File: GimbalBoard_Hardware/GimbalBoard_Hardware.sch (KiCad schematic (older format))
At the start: 5 parts

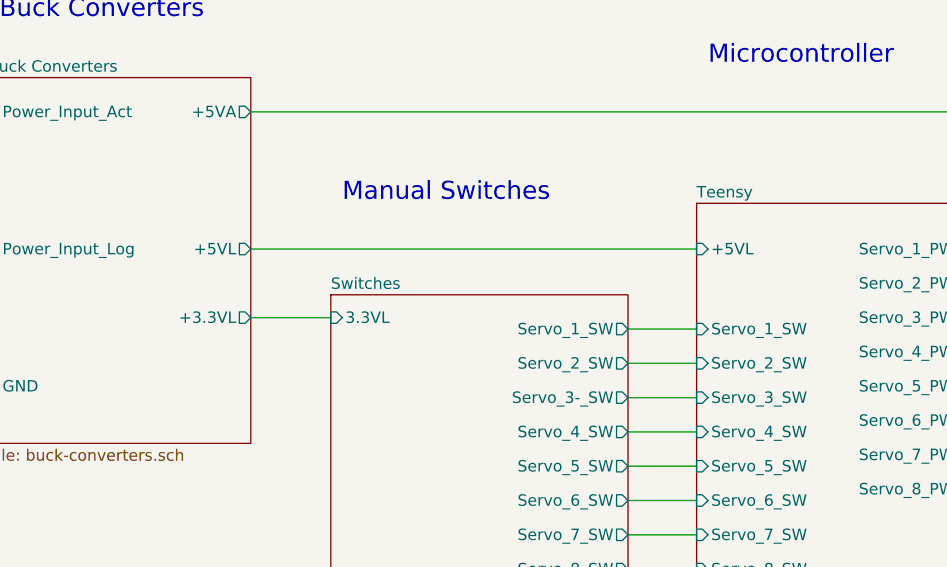
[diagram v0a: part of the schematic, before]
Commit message: now powering the teensy w 3.3VL instead of 5VL
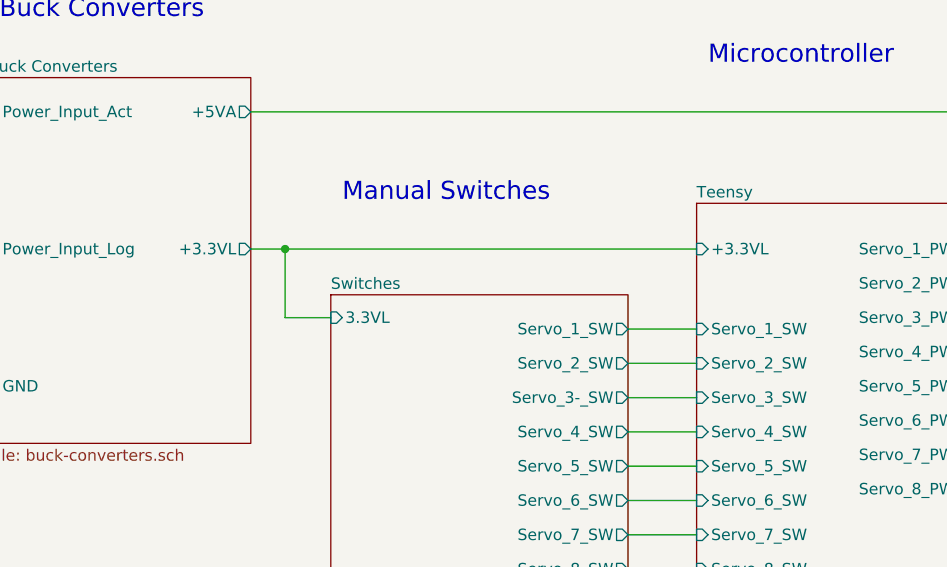
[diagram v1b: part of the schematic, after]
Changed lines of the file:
@@
 F16 "Servo_7_SW" I L 6800 3650 50
 F17 "Servo_8_SW" I L 6800 3800 50
-F18 "+5VL" I L 6800 2400 50
-F19 "Servo_Manual_Control_Right" I L 6800 4300 50
-F20 "Servo_Manual_Control_Left" I L 6800 4150 50
-F21 "GND" I L 6800 4900 50
+F18 "Servo_Manual_Control_Right" I L 6800 4300 50
+F19 "Servo_Manual_Control_Left" I L 6800 4150 50
+F20 "GND" I L 6800 4900 50
+F21 "+3.3VL" I L 6800 2400 50
 $EndSheet
 Wire Wire Line
@@
 	8400 5400 6550 5400
 Wire Wire Line
-	4850 2700 5200 2700
-Wire Wire Line
-	4850 2400 6800 2400
-Wire Wire Line
 	4850 1800 8400 1800
 Wire Wire Line
@@
 Text Notes 8700 1800 0    79   ~ 0
 Servo Connectors
-$Sheet
-S 3700 1650 1150 1600
-U 616B938E
-F0 "Buck Converters" 50
-F1 "buck-converters.sch" 50
-F2 "Power_Input_Act" I L 3700 1800 50
-F3 "+5VL" O R 4850 2400 50
-F4 "+3.3VL" O R 4850 2700 50
-F5 "Power_Input_Log" I L 3700 2400 50
-F6 "GND" I L 3700 3000 50
-F7 "+5VA" O R 4850 1800 50
-$EndSheet
 $Sheet
 S 8700 2100 950  1900
@@
 F11 "GND" I L 8700 3650 50
 $EndSheet
+$Sheet
+S 3700 1650 1150 1600
+U 616B938E
+F0 "Buck Converters" 50
+F1 "buck-converters.sch" 50
+F2 "Power_Input_Act" I L 3700 1800 50
+F3 "+3.3VL" O R 4850 2400 50
+F4 "Power_Input_Log" I L 3700 2400 50
+F5 "GND" I L 3700 3000 50
+F6 "+5VA" O R 4850 1800 50
+$EndSheet
+Wire Wire Line
+	4850 2400 5000 2400
+Wire Wire Line
+	5000 2400 5000 2700
+Wire Wire Line
+	5000 2700 5200 2700
+Connection ~ 5000 2400
+Wire Wire Line
+	5000 2400 6800 2400
 $EndSCHEMATC

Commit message: Added more footprints
I added more footprints. Not done yet. I'd like to come back when when I can verify with max about some of the other components.
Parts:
- D25, D26: footprint (none) -> Diode_SMD:D_0201_0603Metric_Pad0.64x0.40mm_HandSolder
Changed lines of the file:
@@
 F 0 "D25" V 2804 2130 50  0000 L CNN
 F 1 "D_Zener" V 2895 2130 50  0000 L CNN
-F 2 "" H 2850 2050 50  0001 C CNN
+F 2 "Diode_SMD:D_0201_0603Metric_Pad0.64x0.40mm_HandSolder" H 2850 2050 50  0001 C CNN
 F 3 "~" H 2850 2050 50  0001 C CNN
 	1    2850 2050
@@
 F 0 "D26" V 2954 2730 50  0000 L CNN
 F 1 "D_Zener" V 3045 2730 50  0000 L CNN
-F 2 "" H 3000 2650 50  0001 C CNN
+F 2 "Diode_SMD:D_0201_0603Metric_Pad0.64x0.40mm_HandSolder" H 3000 2650 50  0001 C CNN
 F 3 "~" H 3000 2650 50  0001 C CNN
 	1    3000 2650

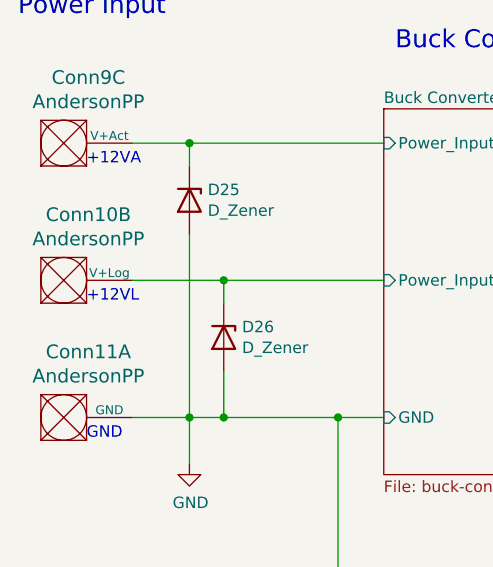
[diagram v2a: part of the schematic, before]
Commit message: Footprints finished
the footprints are finished. the RJ45 connector has been added for eithernet.
the net is in the layout thing but I haven't moved anything yet
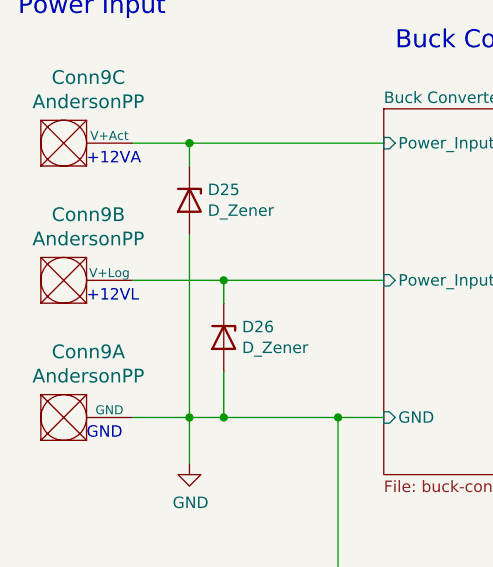
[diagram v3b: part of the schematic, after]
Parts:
- Conn9: footprint (none) -> MRDT_Connectors:Anderson_3_Horizontal_Side_by_Side
- Conn9: renamed from Conn10; footprint (none) -> MRDT_Connectors:Anderson_3_Horizontal_Side_by_Side
- Conn9: renamed from Conn11; footprint (none) -> MRDT_Connectors:Anderson_3_Horizontal_Side_by_Side
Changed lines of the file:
@@
 F 0 "Conn9" H 2408 2287 60  0000 C CNN
 F 1 "AndersonPP" H 2408 2181 60  0000 C CNN
-F 2 "" H 2050 1350 60  0001 C CNN
+F 2 "MRDT_Connectors:Anderson_3_Horizontal_Side_by_Side" H 2050 1350 60  0001 C CNN
 F 3 "" H 2050 1350 60  0001 C CNN
 	3    2200 1900
@@
 $EndComp
 $Comp
-L MRDT_Connectors:AndersonPP Conn10
+L MRDT_Connectors:AndersonPP Conn9
 U 2 1 6159E8BE
 P 2200 2500
-F 0 "Conn10" H 2408 2887 60  0000 C CNN
+F 0 "Conn9" H 2408 2887 60  0000 C CNN
 F 1 "AndersonPP" H 2408 2781 60  0000 C CNN
-F 2 "" H 2050 1950 60  0001 C CNN
+F 2 "MRDT_Connectors:Anderson_3_Horizontal_Side_by_Side" H 2050 1950 60  0001 C CNN
 F 3 "" H 2050 1950 60  0001 C CNN
 	2    2200 2500
@@
 $EndComp
 $Comp
-L MRDT_Connectors:AndersonPP Conn11
+L MRDT_Connectors:AndersonPP Conn9
 U 1 1 6159ED2C
 P 2200 3100
-F 0 "Conn11" H 2408 3487 60  0000 C CNN
+F 0 "Conn9" H 2408 3487 60  0000 C CNN
 F 1 "AndersonPP" H 2408 3381 60  0000 C CNN
-F 2 "" H 2050 2550 60  0001 C CNN
+F 2 "MRDT_Connectors:Anderson_3_Horizontal_Side_by_Side" H 2050 2550 60  0001 C CNN
 F 3 "" H 2050 2550 60  0001 C CNN
 	1    2200 3100

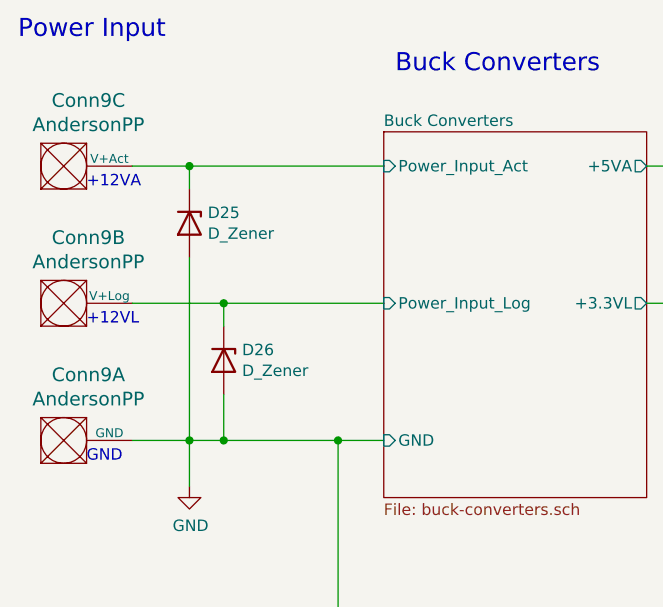
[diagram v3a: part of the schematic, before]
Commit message: ethernet fixed.
the ethernet is fixed. as well as the switch footprint association issue.
I'm not certain that the current footprint being used matches an actual switch. also this edit does not have the 3x2 microfit connectors
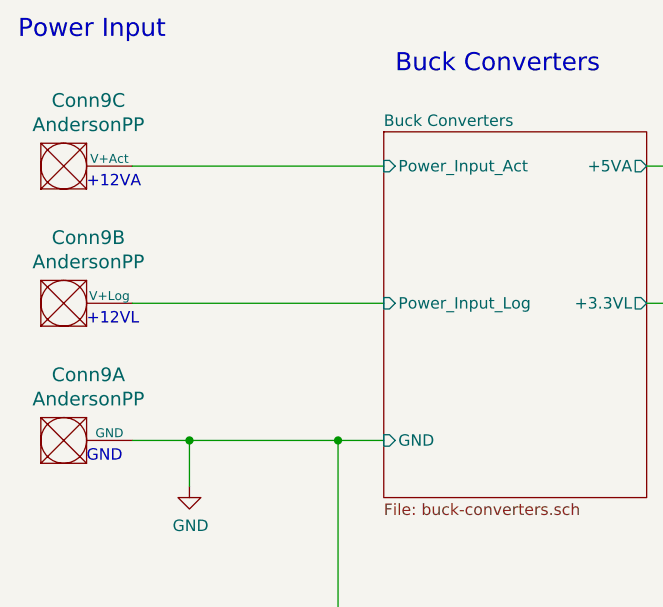
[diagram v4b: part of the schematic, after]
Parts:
- removed D25, D26: D_Zener, Diode_SMD:D_0201_0603Metric_Pad0.64x0.40mm_HandSolder, symbol Device:D_Zener
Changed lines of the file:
@@
 	1    0    0    -1
-$EndComp
-$Comp
-L Device:D_Zener D25
-U 1 1 61614FDE
-P 2850 2050
-F 0 "D25" V 2804 2130 50  0000 L CNN
-F 1 "D_Zener" V 2895 2130 50  0000 L CNN
-F 2 "Diode_SMD:D_0201_0603Metric_Pad0.64x0.40mm_HandSolder" H 2850 2050 50  0001 C CNN
-F 3 "~" H 2850 2050 50  0001 C CNN
-	1    2850 2050
-	0    1    1    0
-$EndComp
-$Comp
-L Device:D_Zener D26
-U 1 1 6161595A
-P 3000 2650
-F 0 "D26" V 2954 2730 50  0000 L CNN
-F 1 "D_Zener" V 3045 2730 50  0000 L CNN
-F 2 "Diode_SMD:D_0201_0603Metric_Pad0.64x0.40mm_HandSolder" H 3000 2650 50  0001 C CNN
-F 3 "~" H 3000 2650 50  0001 C CNN
-	1    3000 2650
-	0    1    1    0
 $EndComp
 $Sheet
@@
 Wire Wire Line
 	2600 3000 2850 3000
-Wire Wire Line
-	2600 1800 2850 1800
-Wire Wire Line
-	2850 1800 2850 1900
-Wire Wire Line
-	2600 2400 3000 2400
-Wire Wire Line
-	2850 2200 2850 3000
 Connection ~ 2850 3000
-Wire Wire Line
-	2850 3000 3000 3000
-Wire Wire Line
-	3000 2400 3000 2500
-Wire Wire Line
-	3000 2800 3000 3000
 Text Notes 2100 1250 0    79   ~ 0
 Power Input
@@
 F21 "+3.3VL" I L 6800 2400 50
 $EndSheet
-Wire Wire Line
-	2850 1800 3700 1800
-Connection ~ 2850 1800
-Wire Wire Line
-	3000 2400 3700 2400
-Connection ~ 3000 2400
-Wire Wire Line
-	3000 3000 3500 3000
-Connection ~ 3000 3000
 Wire Wire Line
 	3500 3000 3500 4550
@@
 Wire Wire Line
 	5000 2400 6800 2400
+Wire Wire Line
+	2600 1800 3700 1800
+Wire Wire Line
+	2600 2400 3700 2400
+Wire Wire Line
+	2850 3000 3500 3000
 $EndSCHEMATC
